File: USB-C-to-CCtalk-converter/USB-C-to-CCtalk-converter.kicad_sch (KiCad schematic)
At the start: 21 parts, among them J1 USB_C_Plug, J4 Conn_01x04, J5 Conn_01x04, Q1 BC847, Q2 BC856, U1 FT230XQ

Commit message: latest updates
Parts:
- renumbered C1 to C10, C2 to C11, C3 to C12, C4 to C13, C5 to C14, C6 to C15, D1 to D3, FB1 to FB2, J1 to J6, J4 to J7, J5 to J8, Q1 to Q3, Q2 to Q4, R3 to R10, R4 to R11, R5 to R12, R6 to R13, R7 to R14, R1 to R8, R2 to R9, U1 to U3

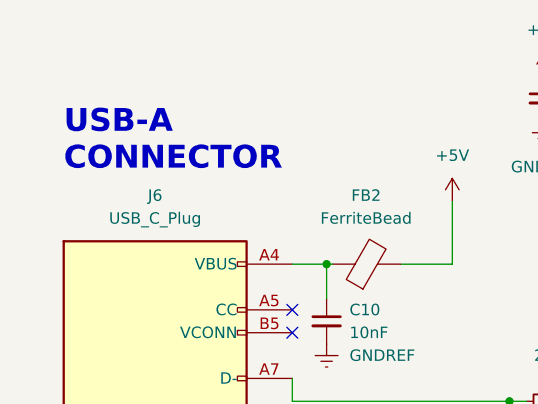
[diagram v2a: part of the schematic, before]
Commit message: add s1u2 dxf bckg and place components
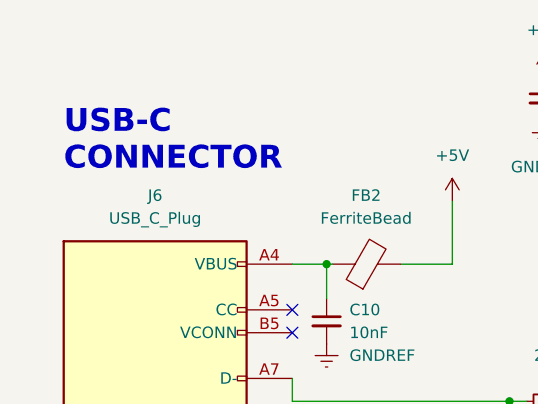
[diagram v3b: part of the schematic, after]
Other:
- note added: "USB-C CONNECTOR"
- note removed: "USB-A CONNECTOR"
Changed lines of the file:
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@@
     (effects (font (size 2.54 2.54)) (justify left bottom))
   )
-  (text "USB-A\nCONNECTOR" (at 20.955 53.34 0)
+  (text "USB-C\nCONNECTOR" (at 20.955 53.34 0)
     (effects (font (size 2.54 2.54) (thickness 0.508) bold) (justify left bottom))
   )
